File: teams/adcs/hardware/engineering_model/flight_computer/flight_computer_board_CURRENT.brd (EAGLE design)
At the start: 90 x 90 mm, 89 parts, among them J1 FEMALE 2x3, U1 Value, U2 Value, U4 TPS732XX, U5 TPS732XX, U6 TPS732XX, U8 TPS732XX

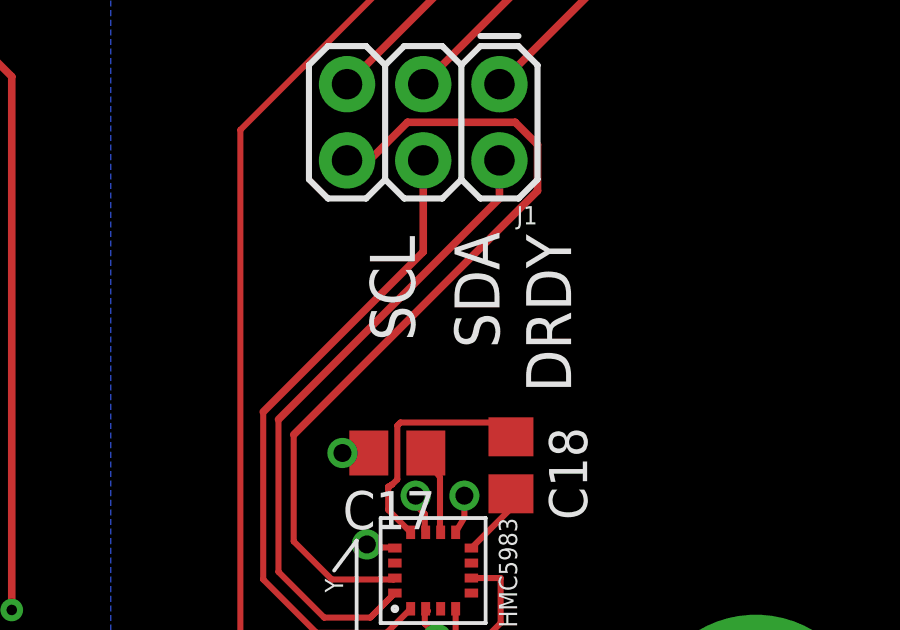
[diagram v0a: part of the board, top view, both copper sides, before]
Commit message: ADCS/FSW: Add on-board documentation
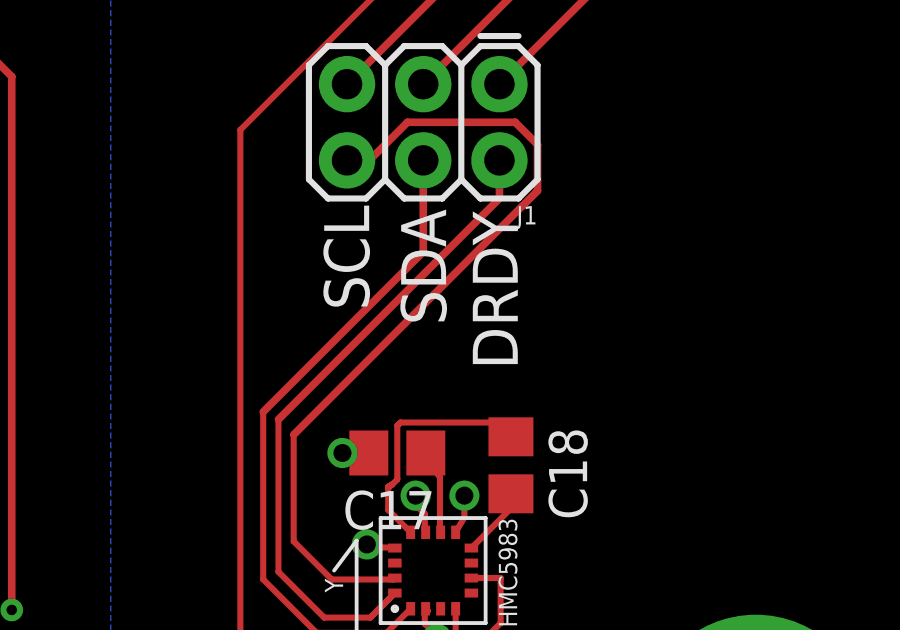
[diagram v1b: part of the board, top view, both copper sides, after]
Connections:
- net N$12 renamed BDOT_RXD
- net N$13 renamed BDOT_TXD
- net N$14 renamed SBWTDIO
- net N$15 renamed SBWTCK
- net N$5 renamed BDOT_P3.5_GPIO_DEBUG
- net N$6 renamed BDOT_P3.4_GPIO_DEBUG
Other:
- board text added: "BCLUART RXD"
- board text added: "BCLUART TXD"
- board text added: "BDOT GND"
- board text added: "BDOT VBAT"
- board text added: "CAN INT"
- board text added: "CAN-INT"
- board text added: "CANH"
- board text added: "CANL"
- board text added: "COMPUTER GND"
- board text added: "COMPUTER VBAT"
- board text added: "I2C SCL"
- board text added: "I2C SDA"
- board text added: "MSP432 (MAIN)"
- board text added: "MSP432 (MPC)"
- board text added: "P3.4 GPIO"
- board text added: "P3.5 GPIO"
- board text added: "RST"
- board text added: "RXD"
- board text added: "SBWTCK"
- board text added: "SBWTDIO"
- board text added: "SCL (SENSOR)"
- board text added: "SDA (SENSOR)"
- board text added: "SPI CLK"
- board text added: "SPI CS"
- board text added: "SPI MISO"
- board text added: "SPI MOSI"
- board text added: "SYNC1"
- board text added: "SYNC2"
- board text added: "TCK SWDCL"
- board text added: "TCK SWDCLK"
- board text added: "TDI"
- board text added: "TDO"
- board text added: "TMS SWDIO"
- board text added: "TXD"
- board text added: "UART RXD"
- board text added: "UART TXD"
